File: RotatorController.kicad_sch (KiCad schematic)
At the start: 58 parts, among them J1 USB_A, J2 Rotator, J4 Motor Cap, K1 G5LE-1, K2 G5LE-1, K3 G5LE-1, Q1 BSS123, Q2 BSS123, Q3 BSS123, SW1 CW, SW2 CW, U1 Teensy4.0, U3 AP2161W

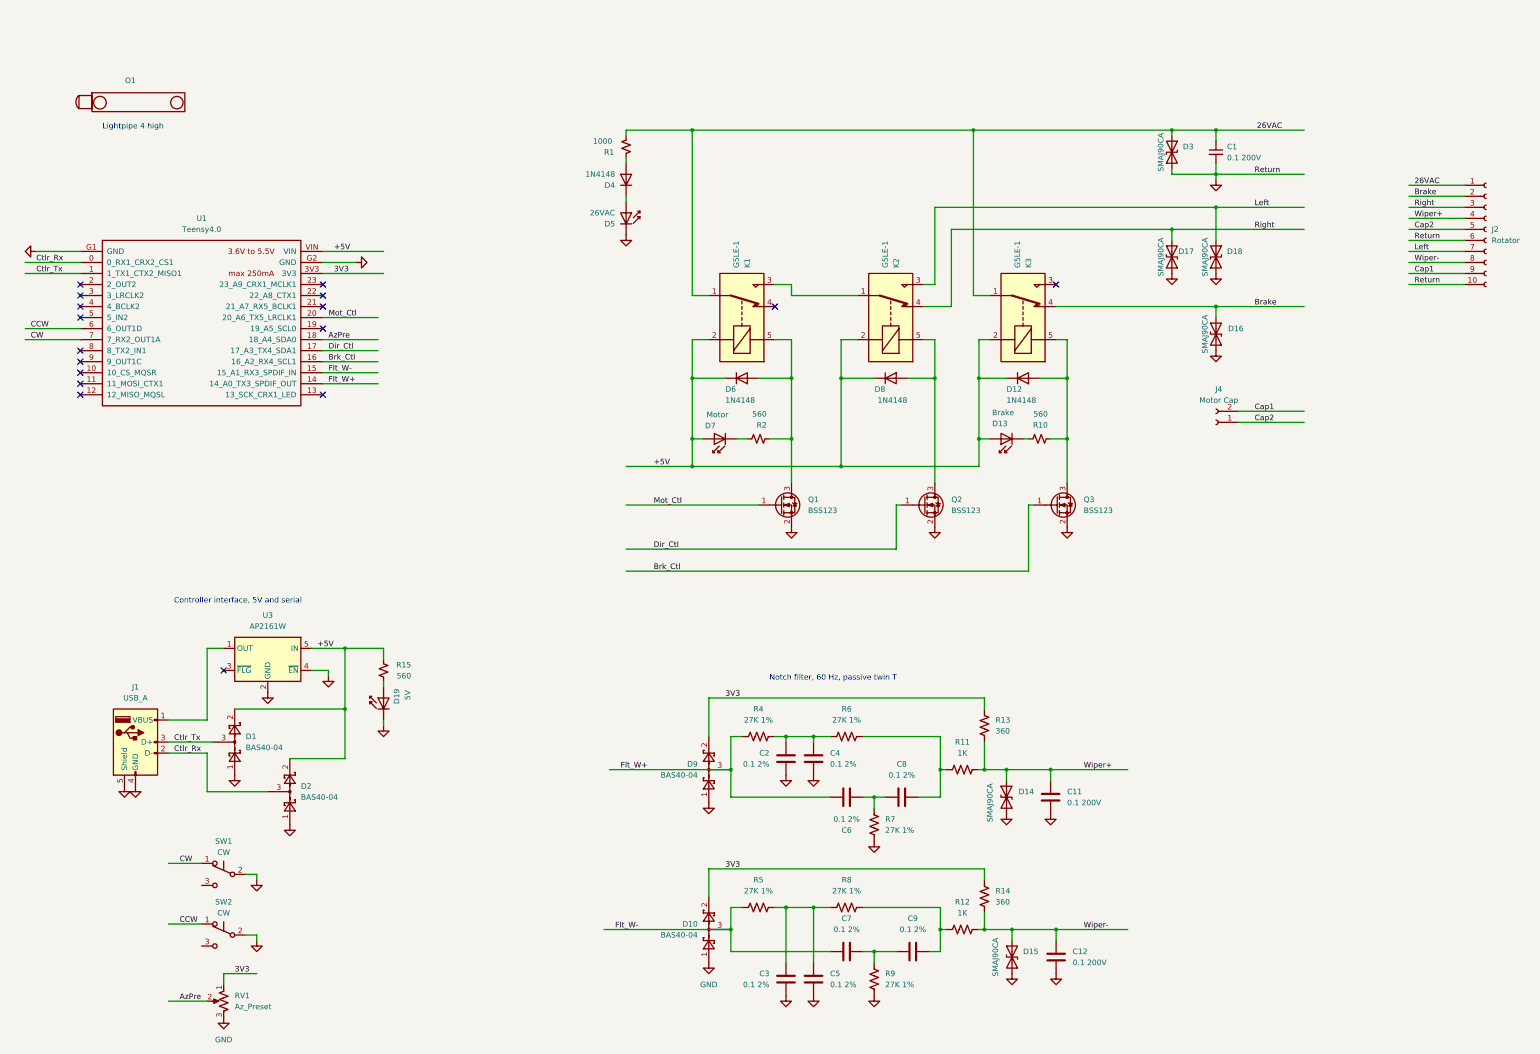
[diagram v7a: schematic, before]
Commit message: added tag for release, KiCAD updated the dates, but no intended changes
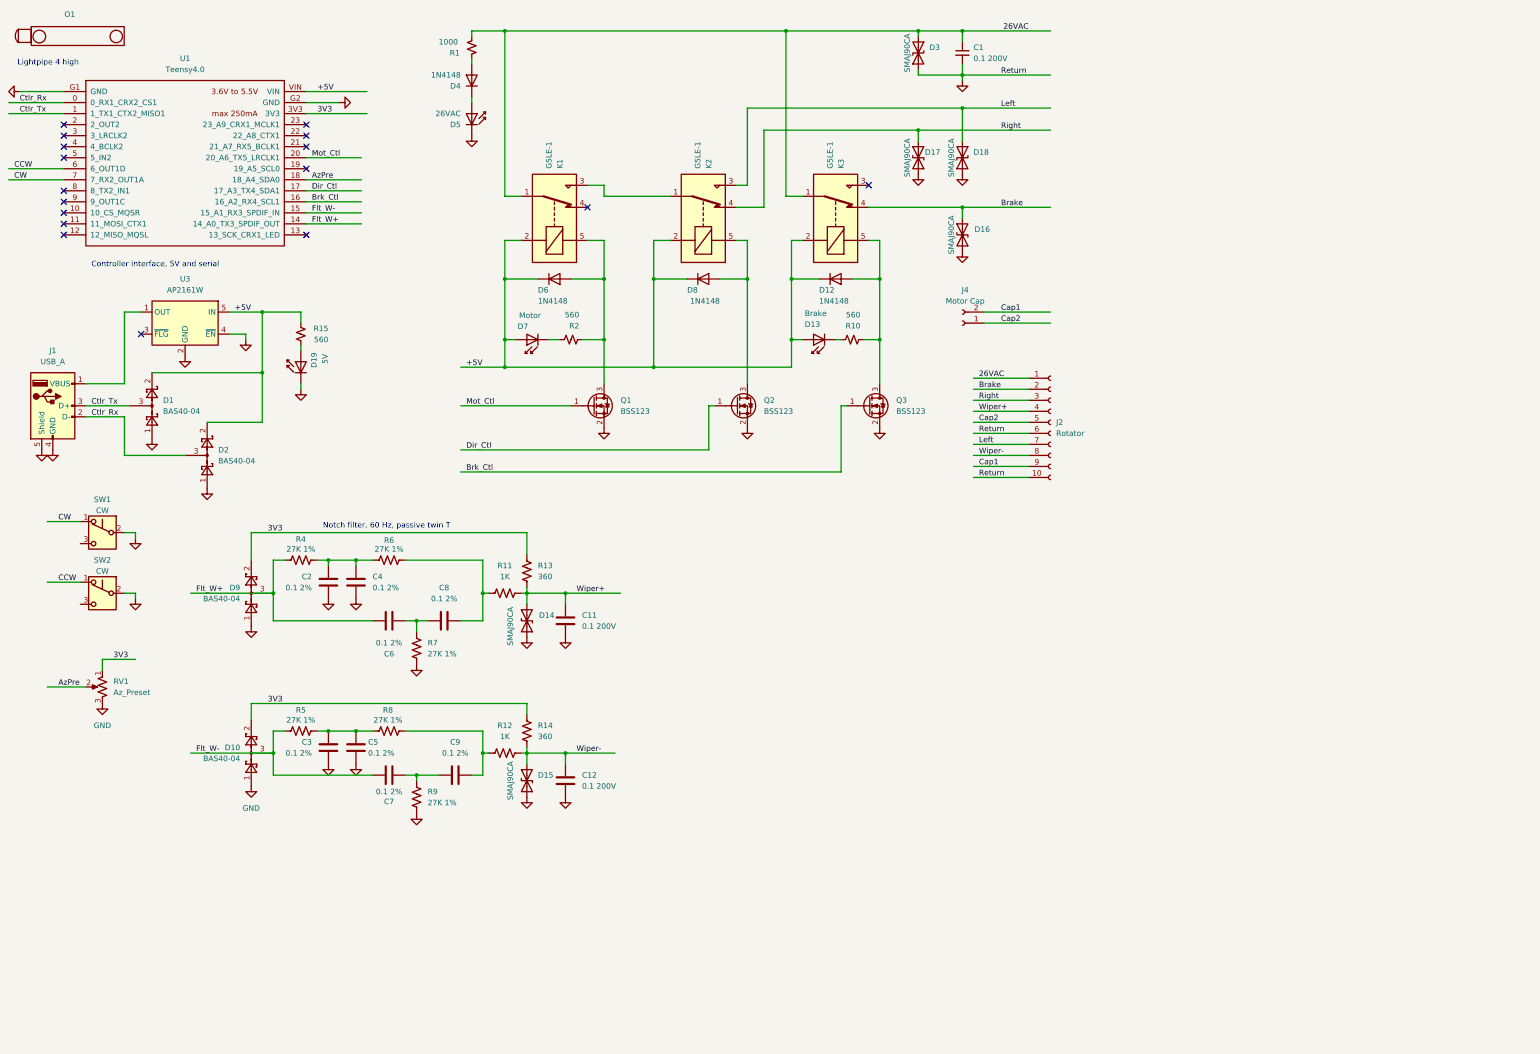
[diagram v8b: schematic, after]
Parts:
- D12, D4, D6, D8: footprint Diode_SMD:D_SOD-123F -> Diode_THT:D_DO-35_SOD27_P7.62mm_Horizontal
- D13, D19, D5, D7: footprint LED_SMD:LED_miniPLCC_2315_Handsoldering -> LED_THT:LED_D3.0mm_IRBlack
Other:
- moved on the sheet: C1, C11, C12, C2, C3, C4, C5, C6, C7, C8, C9, D1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
